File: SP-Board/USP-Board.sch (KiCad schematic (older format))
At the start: 10 parts

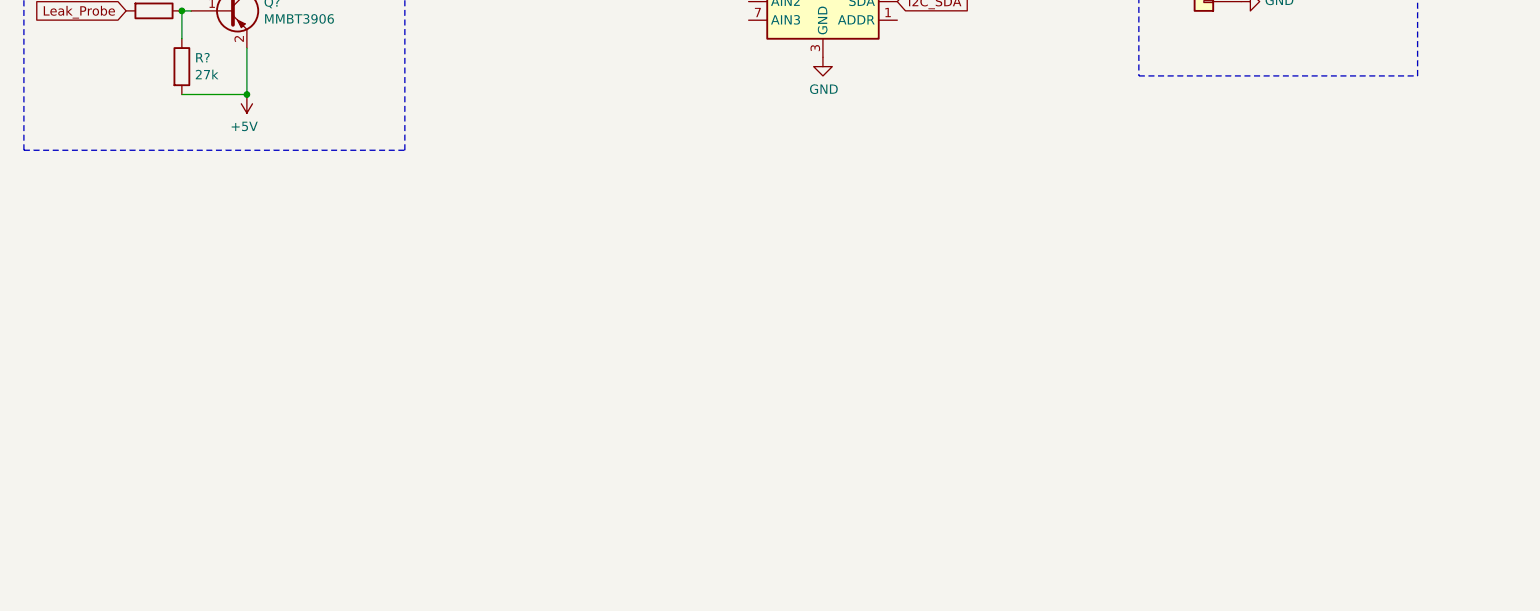
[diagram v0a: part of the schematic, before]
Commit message: Added Leak probe connectors and xt60 connector
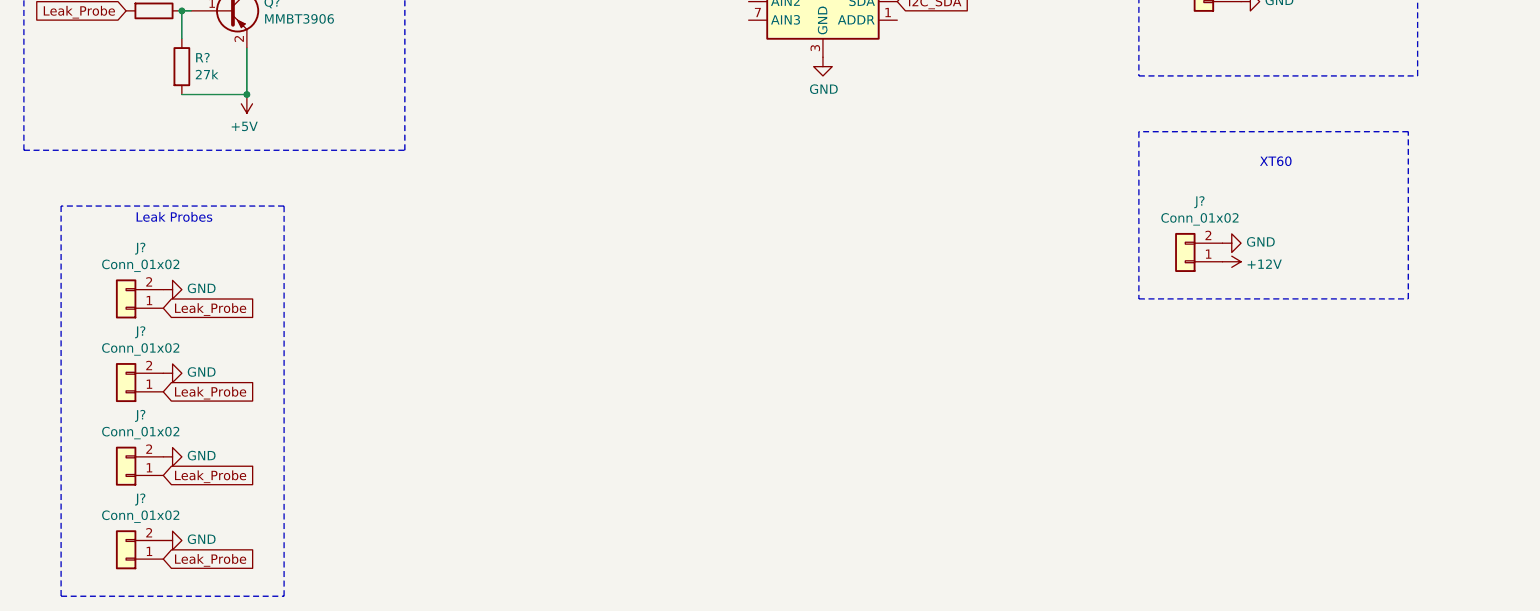
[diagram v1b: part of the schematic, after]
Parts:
- added J? (x5): Conn_01x02, symbol Connector_Generic:Conn_01x02
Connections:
- net GND: now also J?.2 (Pin_2), J?.2 (Pin_2), J?.2 (Pin_2), J?.2 (Pin_2), J?.2 (Pin_2)
- net Leak_Probe: now also J?.1 (Pin_1), J?.1 (Pin_1), J?.1 (Pin_1), J?.1 (Pin_1)
- new net +12V: J?.1 (Pin_1)
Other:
- note added: "Leak Probes\n"
- note added: "XT60\n"
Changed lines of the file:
@@
 Text Notes 7450 1350 0    50   ~ 0
 Depht/Temp\n
+$Comp
+L Connector_Generic:Conn_01x02 J?
+U 1 1 5C6F22AD
+P 7200 3450
+F 0 "J?" H 7120 3125 50  0000 C CNN
+F 1 "Conn_01x02" H 7120 3216 50  0000 C CNN
+F 2 "" H 7200 3450 50  0001 C CNN
+F 3 "~" H 7200 3450 50  0001 C CNN
+	1    7200 3450
+	-1   0    0    1
+$EndComp
+$Comp
+L power:GND #PWR?
+U 1 1 5C6F2330
+P 7400 3350
+F 0 "#PWR?" H 7400 3100 50  0001 C CNN
+F 1 "GND" V 7405 3222 50  0000 R CNN
+F 2 "" H 7400 3350 50  0001 C CNN
+F 3 "" H 7400 3350 50  0001 C CNN
+	1    7400 3350
+	0    -1   -1   0
+$EndComp
+$Comp
+L power:+12V #PWR?
+U 1 1 5C6F23A3
+P 7400 3450
+F 0 "#PWR?" H 7400 3300 50  0001 C CNN
+F 1 "+12V" V 7415 3578 50  0000 L CNN
+F 2 "" H 7400 3450 50  0001 C CNN
+F 3 "" H 7400 3450 50  0001 C CNN
+	1    7400 3450
+	0    1    1    0
+$EndComp
+Wire Notes Line
+	6950 3650 8400 3650
+Wire Notes Line
+	8400 3650 8400 2750
+Wire Notes Line
+	8400 2750 6950 2750
+Wire Notes Line
+	6950 2750 6950 3650
+Text Notes 7600 2950 0    50   ~ 0
+XT60\n
+$Comp
+L Connector_Generic:Conn_01x02 J?
+U 1 1 5C6F2A9B
+P 1500 3700
+F 0 "J?" H 1420 3375 50  0000 C CNN
+F 1 "Conn_01x02" H 1420 3466 50  0000 C CNN
+F 2 "" H 1500 3700 50  0001 C CNN
+F 3 "~" H 1500 3700 50  0001 C CNN
+	1    1500 3700
+	-1   0    0    1
+$EndComp
+$Comp
+L Connector_Generic:Conn_01x02 J?
+U 1 1 5C6F2AFB
+P 1500 4150
+F 0 "J?" H 1420 3825 50  0000 C CNN
+F 1 "Conn_01x02" H 1420 3916 50  0000 C CNN
+F 2 "" H 1500 4150 50  0001 C CNN
+F 3 "~" H 1500 4150 50  0001 C CNN
+	1    1500 4150
+	-1   0    0    1
+$EndComp
+$Comp
+L Connector_Generic:Conn_01x02 J?
+U 1 1 5C6F2B6A
+P 1500 4600
+F 0 "J?" H 1420 4275 50  0000 C CNN
+F 1 "Conn_01x02" H 1420 4366 50  0000 C CNN
+F 2 "" H 1500 4600 50  0001 C CNN
+F 3 "~" H 1500 4600 50  0001 C CNN
+	1    1500 4600
+	-1   0    0    1
+$EndComp
+$Comp
+L Connector_Generic:Conn_01x02 J?
+U 1 1 5C6F2BA4
+P 1500 5050
+F 0 "J?" H 1420 4725 50  0000 C CNN
+F 1 "Conn_01x02" H 1420 4816 50  0000 C CNN
+F 2 "" H 1500 5050 50  0001 C CNN
+F 3 "~" H 1500 5050 50  0001 C CNN
+	1    1500 5050
+	-1   0    0    1
+$EndComp
+Text GLabel 1700 3700 2    50   Input ~ 0
+Leak_Probe
+Text GLabel 1700 4150 2    50   Input ~ 0
+Leak_Probe
+Text GLabel 1700 4600 2    50   Input ~ 0
+Leak_Probe
+Text GLabel 1700 5050 2    50   Input ~ 0
+Leak_Probe
+$Comp
+L power:GND #PWR?
+U 1 1 5C6F390D
+P 1700 4500
+F 0 "#PWR?" H 1700 4250 50  0001 C CNN
+F 1 "GND" V 1705 4372 50  0000 R CNN
+F 2 "" H 1700 4500 50  0001 C CNN
+F 3 "" H 1700 4500 50  0001 C CNN
+	1    1700 4500
+	0    -1   -1   0
+$EndComp
+$Comp
+L power:GND #PWR?
+U 1 1 5C6F396A
+P 1700 4050
+F 0 "#PWR?" H 1700 3800 50  0001 C CNN
+F 1 "GND" V 1705 3922 50  0000 R CNN
+F 2 "" H 1700 4050 50  0001 C CNN
+F 3 "" H 1700 4050 50  0001 C CNN
+	1    1700 4050
+	0    -1   -1   0
+$EndComp
+$Comp
+L power:GND #PWR?
+U 1 1 5C6F3993
+P 1700 3600
+F 0 "#PWR?" H 1700 3350 50  0001 C CNN
+F 1 "GND" V 1705 3472 50  0000 R CNN
+F 2 "" H 1700 3600 50  0001 C CNN
+F 3 "" H 1700 3600 50  0001 C CNN
+	1    1700 3600
+	0    -1   -1   0
+$EndComp
+$Comp
+L power:GND #PWR?
+U 1 1 5C6F39BC
+P 1700 4950
+F 0 "#PWR?" H 1700 4700 50  0001 C CNN
+F 1 "GND" V 1705 4822 50  0000 R CNN
+F 2 "" H 1700 4950 50  0001 C CNN
+F 3 "" H 1700 4950 50  0001 C CNN
+	1    1700 4950
+	0    -1   -1   0
+$EndComp
+Wire Notes Line
+	1150 5250 2350 5250
+Wire Notes Line
+	2350 5250 2350 3150
+Wire Notes Line
+	2350 3150 1150 3150
+Wire Notes Line
+	1150 3150 1150 5250
+Text Notes 1550 3250 0    50   ~ 0
+Leak Probes\n
 $EndSCHEMATC

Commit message: moving macines
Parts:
- added C?: C_Small, symbol Device:C_Small
- added J? (x2): Conn_01x03, symbol Connector_Generic:Conn_01x03
- added J?: Conn_01x04, symbol Connector_Generic:Conn_01x04
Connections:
- net +12V: now also J?.1 (Pin_1), J?.3 (Pin_3)
- net +5V: now also U?.8 (VDD), C?.2
- net EXT_PWM_LED: now also J?.2 (Pin_2)
- net GND: now also C?.1, J?.1 (Pin_1), J?.2 (Pin_2), J?.2 (Pin_2)
- net I2C_SCL: now also J?.3 (Pin_3)
- net I2C_SDA: now also J?.4 (Pin_4)
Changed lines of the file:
@@
 U 1 1 5C6DF5CB
 P 5250 1950
-F 0 "U?" H 5250 2628 50  0000 C CNN
-F 1 "ADS1015IDGS" H 5250 2537 50  0000 C CNN
+F 0 "U?" H 4850 2650 50  0000 C CNN
+F 1 "ADS1015IDGS" H 4850 2550 50  0000 C CNN
 F 2 "Package_SO:TSSOP-10_3x3mm_P0.5mm" H 5250 1450 50  0001 C CNN
 F 3 "http://www.ti.com/lit/ds/symlink/ads1015.pdf" H 5200 1050 50  0001 C CNN
@@
 Text Notes 1550 3250 0    50   ~ 0
 Leak Probes\n
+$Comp
+L Connector_Generic:Conn_01x03 J?
+U 1 1 5C6F621E
+P 7200 4550
+F 0 "J?" H 7120 4225 50  0000 C CNN
+F 1 "Conn_01x03" H 7120 4316 50  0000 C CNN
+F 2 "" H 7200 4550 50  0001 C CNN
+F 3 "~" H 7200 4550 50  0001 C CNN
+	1    7200 4550
+	-1   0    0    1
+$EndComp
+$Comp
+L power:GND #PWR?
+U 1 1 5C6F62AC
+P 7400 4650
+F 0 "#PWR?" H 7400 4400 50  0001 C CNN
+F 1 "GND" V 7405 4522 50  0000 R CNN
+F 2 "" H 7400 4650 50  0001 C CNN
+F 3 "" H 7400 4650 50  0001 C CNN
+	1    7400 4650
+	0    -1   -1   0
+$EndComp
+$Comp
+L power:+12V #PWR?
+U 1 1 5C6F6333
+P 7400 4450
+F 0 "#PWR?" H 7400 4300 50  0001 C CNN
+F 1 "+12V" V 7415 4578 50  0000 L CNN
+F 2 "" H 7400 4450 50  0001 C CNN
+F 3 "" H 7400 4450 50  0001 C CNN
+	1    7400 4450
+	0    1    1    0
+$EndComp
+Text GLabel 7400 4550 2    50   Input ~ 0
+EXT_PWM_LED
+$Comp
+L Connector_Generic:Conn_01x04 J?
+U 1 1 5C6F63B5
+P 7200 5400
+F 0 "J?" H 7120 4975 50  0000 C CNN
+F 1 "Conn_01x04" H 7120 5066 50  0000 C CNN
+F 2 "" H 7200 5400 50  0001 C CNN
+F 3 "~" H 7200 5400 50  0001 C CNN
+	1    7200 5400
+	-1   0    0    1
+$EndComp
+Text GLabel 7400 5200 2    50   Input ~ 0
+I2C_SDA
+Text GLabel 7400 5300 2    50   Input ~ 0
+I2C_SCL
+$Comp
+L power:GND #PWR?
+U 1 1 5C6F6B79
+P 7400 5400
+F 0 "#PWR?" H 7400 5150 50  0001 C CNN
+F 1 "GND" V 7405 5272 50  0000 R CNN
+F 2 "" H 7400 5400 50  0001 C CNN
+F 3 "" H 7400 5400 50  0001 C CNN
+	1    7400 5400
+	0    -1   -1   0
+$EndComp
+$Comp
+L power:+12V #PWR?
+U 1 1 5C6F6BA6
+P 7400 5500
+F 0 "#PWR?" H 7400 5350 50  0001 C CNN
+F 1 "+12V" V 7415 5628 50  0000 L CNN
+F 2 "" H 7400 5500 50  0001 C CNN
+F 3 "" H 7400 5500 50  0001 C CNN
+	1    7400 5500
+	0    1    1    0
+$EndComp
+$Comp
+L Connector_Generic:Conn_01x03 J?
+U 1 1 5C6F7BD4
+P 7200 6050
+F 0 "J?" H 7120 5725 50  0000 C CNN
+F 1 "Conn_01x03" H 7120 5816 50  0000 C CNN
+F 2 "" H 7200 6050 50  0001 C CNN
+F 3 "~" H 7200 6050 50  0001 C CNN
+	1    7200 6050
+	-1   0    0    1
+$EndComp
+$Comp
+L power:GND #PWR?
+U 1 1 5C6F7CC0
+P 7400 6050
+F 0 "#PWR?" H 7400 5800 50  0001 C CNN
+F 1 "GND" V 7400 5850 50  0000 C CNN
+F 2 "" H 7400 6050 50  0001 C CNN
+F 3 "" H 7400 6050 50  0001 C CNN
+	1    7400 6050
+	0    -1   -1   0
+$EndComp
+$Comp
+L Device:C_Small C?
+U 1 1 5C6F8556
+P 5250 1250
+F 0 "C?" H 5342 1296 50  0000 L CNN
+F 1 "C_Small" H 5342 1205 50  0000 L CNN
+F 2 "" H 5250 1250 50  0001 C CNN
+F 3 "~" H 5250 1250 50  0001 C CNN
+	1    5250 1250
+	1    0    0    -1
+$EndComp
+Wire Wire Line
+	5250 1350 5250 1400
+$Comp
+L power:GND #PWR?
+U 1 1 5C6F8BB7
+P 5250 1150
+F 0 "#PWR?" H 5250 900 50  0001 C CNN
+F 1 "GND" H 5255 977 50  0000 C CNN
+F 2 "" H 5250 1150 50  0001 C CNN
+F 3 "" H 5250 1150 50  0001 C CNN
+	1    5250 1150
+	-1   0    0    1
+$EndComp
+$Comp
+L power:+5V #PWR?
+U 1 1 5C6F8C33
+P 5450 1400
+F 0 "#PWR?" H 5450 1250 50  0001 C CNN
+F 1 "+5V" V 5465 1528 50  0000 L CNN
+F 2 "" H 5450 1400 50  0001 C CNN
+F 3 "" H 5450 1400 50  0001 C CNN
+	1    5450 1400
+	0    1    1    0
+$EndComp
+Wire Wire Line
+	5450 1400 5250 1400
+Connection ~ 5250 1400
+Wire Wire Line
+	5250 1400 5250 1450
 $EndSCHEMATC

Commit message: Udated ADC 90% complete
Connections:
- net I2C_SDA: now also U?.1 (ADDR)
- net Leak_Sig: now also U?.5 (AIN1)
- net ANLG_Induction_SENS: now reaches U?.4 (AIN0)
- net ANLG_Induction_SENS: now also J?.3 (Pin_3)
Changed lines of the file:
@@
 Wire Wire Line
 	5250 1400 5250 1450
+Text GLabel 5650 2150 2    50   Input ~ 0
+I2C_SDA
+Text GLabel 7400 5950 2    50   Input ~ 0
+ANLG_Induction_SENS
+Text GLabel 4850 1850 0    50   Input ~ 0
+ANLG_Induction_SENS
+Text GLabel 4850 1950 0    50   Input ~ 0
+Leak_Sig
 $EndSCHEMATC

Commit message: backup
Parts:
- added H1, H2, H3, H4: MountingHole, MountingHole:MountingHole_3mm_Pad, symbol Mechanical:MountingHole
- J10, J11: renamed from J?; footprint (none) -> Blue_ESC:RJ45_8
- gave numbers to parts that had none: 17

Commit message: More sch updates
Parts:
- added C2, C3, C4, C5, C6: 1uF, symbol Device:CP
- added U2: MAX232, symbol Interface_UART:MAX232
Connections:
- net +5V: now also J8.1 (Pin_1)
- net GND: now also J8.3 (Pin_3), C3.2, C6.1, U2.15 (GND); no longer J8.2 (Pin_2)
- net ANLG_Induction_SENS renamed ANLG_HAL_SENS
- net ANLG_HAL_SENS: now also J8.2 (Pin_2); no longer J8.3 (Pin_3)
- new net: C2.1, U2.1 (C1+)
- new net: C3.1, C4.2, U2.16 (VCC)
- new net: C4.1, U2.2 (VS+)
- new net: C2.2, U2.3 (C1-)
- new net: C5.1, U2.4 (C2+)
- new net: C5.2, U2.5 (C2-)
- new net: C6.2, U2.6 (VS-)
- no-connect marks 0 -> 3
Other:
- moved on the sheet: H1, H2, H3, H4
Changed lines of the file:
@@
 L power:GND #PWR0122
 U 1 1 5C6F7CC0
-P 7400 6050
-F 0 "#PWR0122" H 7400 5800 50  0001 C CNN
-F 1 "GND" V 7400 5850 50  0000 C CNN
-F 2 "" H 7400 6050 50  0001 C CNN
-F 3 "" H 7400 6050 50  0001 C CNN
-	1    7400 6050
+P 7400 5950
+F 0 "#PWR0122" H 7400 5700 50  0001 C CNN
+F 1 "GND" V 7400 5750 50  0000 C CNN
+F 2 "" H 7400 5950 50  0001 C CNN
+F 3 "" H 7400 5950 50  0001 C CNN
+	1    7400 5950
 	0    -1   -1   0
 $EndComp
@@
 Text GLabel 5650 2150 2    50   Input ~ 0
 I2C_SDA
-Text GLabel 7400 5950 2    50   Input ~ 0
-ANLG_Induction_SENS
+Text GLabel 7400 6050 2    50   Input ~ 0
+ANLG_HAL_SENS
 Text GLabel 4850 1850 0    50   Input ~ 0
-ANLG_Induction_SENS
+ANLG_HAL_SENS
 Text GLabel 4850 1950 0    50   Input ~ 0
 Leak_Sig
@@
 L Mechanical:MountingHole H1
 U 1 1 5C84499E
-P 4750 4950
-F 0 "H1" H 4850 4996 50  0000 L CNN
-F 1 "MountingHole" H 4850 4905 50  0000 L CNN
-F 2 "MountingHole:MountingHole_3mm_Pad" H 4750 4950 50  0001 C CNN
-F 3 "~" H 4750 4950 50  0001 C CNN
-	1    4750 4950
+P 1200 6150
+F 0 "H1" H 1300 6196 50  0000 L CNN
+F 1 "MountingHole" H 1300 6105 50  0000 L CNN
+F 2 "MountingHole:MountingHole_3mm_Pad" H 1200 6150 50  0001 C CNN
+F 3 "~" H 1200 6150 50  0001 C CNN
+	1    1200 6150
 	1    0    0    -1
 $EndComp
@@
 L Mechanical:MountingHole H2
 U 1 1 5C8449DE
-P 4750 5300
-F 0 "H2" H 4850 5346 50  0000 L CNN
-F 1 "MountingHole" H 4850 5255 50  0000 L CNN
-F 2 "MountingHole:MountingHole_3mm_Pad" H 4750 5300 50  0001 C CNN
-F 3 "~" H 4750 5300 50  0001 C CNN
-	1    4750 5300
+P 1200 6500
+F 0 "H2" H 1300 6546 50  0000 L CNN
+F 1 "MountingHole" H 1300 6455 50  0000 L CNN
+F 2 "MountingHole:MountingHole_3mm_Pad" H 1200 6500 50  0001 C CNN
+F 3 "~" H 1200 6500 50  0001 C CNN
+	1    1200 6500
 	1    0    0    -1
 $EndComp
@@
 L Mechanical:MountingHole H3
 U 1 1 5C844A42
-P 4750 5700
-F 0 "H3" H 4850 5746 50  0000 L CNN
-F 1 "MountingHole" H 4850 5655 50  0000 L CNN
-F 2 "MountingHole:MountingHole_3mm_Pad" H 4750 5700 50  0001 C CNN
-F 3 "~" H 4750 5700 50  0001 C CNN
-	1    4750 5700
+P 1200 6900
+F 0 "H3" H 1300 6946 50  0000 L CNN
+F 1 "MountingHole" H 1300 6855 50  0000 L CNN
+F 2 "MountingHole:MountingHole_3mm_Pad" H 1200 6900 50  0001 C CNN
+F 3 "~" H 1200 6900 50  0001 C CNN
+	1    1200 6900
 	1    0    0    -1
 $EndComp
@@
 L Mechanical:MountingHole H4
 U 1 1 5C844AA4
-P 4750 6000
-F 0 "H4" H 4850 6046 50  0000 L CNN
-F 1 "MountingHole" H 4850 5955 50  0000 L CNN
-F 2 "MountingHole:MountingHole_3mm_Pad" H 4750 6000 50  0001 C CNN
-F 3 "~" H 4750 6000 50  0001 C CNN
-	1    4750 6000
-	1    0    0    -1
-$EndComp
+P 1200 7200
+F 0 "H4" H 1300 7246 50  0000 L CNN
+F 1 "MountingHole" H 1300 7155 50  0000 L CNN
+F 2 "MountingHole:MountingHole_3mm_Pad" H 1200 7200 50  0001 C CNN
+F 3 "~" H 1200 7200 50  0001 C CNN
+	1    1200 7200
+	1    0    0    -1
+$EndComp
+$Comp
+L power:+5V #PWR0125
+U 1 1 5C998D8E
+P 7400 6150
+F 0 "#PWR0125" H 7400 6000 50  0001 C CNN
+F 1 "+5V" V 7415 6278 50  0000 L CNN
+F 2 "" H 7400 6150 50  0001 C CNN
+F 3 "" H 7400 6150 50  0001 C CNN
+	1    7400 6150
+	0    1    1    0
+$EndComp
+NoConn ~ 5650 1750
+NoConn ~ 4850 2050
+NoConn ~ 4850 2150
+$Comp
+L Interface_UART:MAX232 U2
+U 1 1 5C99D6CE
+P 4250 5750
+F 0 "U2" H 4000 4700 50  0000 C CNN
+F 1 "MAX232" H 4050 6800 50  0000 C CNN
+F 2 "" H 4300 4700 50  0001 L CNN
+F 3 "http://www.ti.com/lit/ds/symlink/max232.pdf" H 4250 5850 50  0001 C CNN
+	1    4250 5750
+	1    0    0    -1
+$EndComp
+$Comp
+L Device:CP C2
+U 1 1 5C99E1C6
+P 3250 5000
+F 0 "C2" H 3368 5046 50  0000 L CNN
+F 1 "1uF" H 3368 4955 50  0000 L CNN
+F 2 "" H 3288 4850 50  0001 C CNN
+F 3 "~" H 3250 5000 50  0001 C CNN
+	1    3250 5000
+	1    0    0    -1
+$EndComp
+Wire Wire Line
+	3450 4850 3250 4850
+Wire Wire Line
+	3250 5150 3450 5150
+$Comp
+L power:GND #PWR0126
+U 1 1 5C99E75A
+P 4250 6950
+F 0 "#PWR0126" H 4250 6700 50  0001 C CNN
+F 1 "GND" H 4255 6777 50  0000 C CNN
+F 2 "" H 4250 6950 50  0001 C CNN
+F 3 "" H 4250 6950 50  0001 C CNN
+	1    4250 6950
+	1    0    0    -1
+$EndComp
+$Comp
+L Device:CP C6
+U 1 1 5C99E79E
+P 5750 5650
+F 0 "C6" V 5495 5650 50  0000 C CNN
+F 1 "1uF" V 5586 5650 50  0000 C CNN
+F 2 "" H 5788 5500 50  0001 C CNN
+F 3 "~" H 5750 5650 50  0001 C CNN
+	1    5750 5650
+	0    1    1    0
+$EndComp
+Wire Wire Line
+	5600 5650 5050 5650
+$Comp
+L power:GND #PWR0127
+U 1 1 5C99EAE5
+P 5900 5650
+F 0 "#PWR0127" H 5900 5400 50  0001 C CNN
+F 1 "GND" H 5905 5477 50  0000 C CNN
+F 2 "" H 5900 5650 50  0001 C CNN
+F 3 "" H 5900 5650 50  0001 C CNN
+	1    5900 5650
+	1    0    0    -1
+$EndComp
+$Comp
+L power:GND #PWR0128
+U 1 1 5C99EB24
+P 3250 4200
+F 0 "#PWR0128" H 3250 3950 50  0001 C CNN
+F 1 "GND" H 3255 4027 50  0000 C CNN
+F 2 "" H 3250 4200 50  0001 C CNN
+F 3 "" H 3250 4200 50  0001 C CNN
+	1    3250 4200
+	1    0    0    -1
+$EndComp
+$Comp
+L Device:CP C5
+U 1 1 5C99EB63
+P 5200 5000
+F 0 "C5" H 5318 5046 50  0000 L CNN
+F 1 "1uF" H 5318 4955 50  0000 L CNN
+F 2 "" H 5238 4850 50  0001 C CNN
+F 3 "~" H 5200 5000 50  0001 C CNN
+	1    5200 5000
+	1    0    0    -1
+$EndComp
+Wire Wire Line
+	5200 4850 5050 4850
+Wire Wire Line
+	5200 5150 5050 5150
+Wire Wire Line
+	5050 5350 5550 5350
+Wire Wire Line
+	5550 5350 5550 4200
+Wire Wire Line
+	5550 4200 4850 4200
+$Comp
+L Device:CP C4
+U 1 1 5C99F2B9
+P 4700 4200
+F 0 "C4" V 4445 4200 50  0000 C CNN
+F 1 "1uF" V 4536 4200 50  0000 C CNN
+F 2 "" H 4738 4050 50  0001 C CNN
+F 3 "~" H 4700 4200 50  0001 C CNN
+	1    4700 4200
+	0    1    1    0
+$EndComp
+Wire Wire Line
+	4250 4550 4250 4200
+Wire Wire Line
+	4250 4200 4550 4200
+$Comp
+L Device:CP C3
+U 1 1 5C99F6D7
+P 3400 4200
+F 0 "C3" V 3145 4200 50  0000 C CNN
+F 1 "1uF" V 3236 4200 50  0000 C CNN
+F 2 "" H 3438 4050 50  0001 C CNN
+F 3 "~" H 3400 4200 50  0001 C CNN
+	1    3400 4200
+	0    1    1    0
+$EndComp
+Wire Wire Line
+	3550 4200 4250 4200
+Connection ~ 4250 4200
 $EndSCHEMATC

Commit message: Early Footprint
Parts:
- C2, C3, C4, C5, C6: footprint (none) -> Capacitor_Tantalum_SMD:CP_EIA-1608-08_AVX-J_Pad1.25x1.05mm_HandSolder
- D1: footprint (none) -> LED_SMD:LED_0603_1608Metric
- R1, R2, R3: footprint (none) -> Resistor_SMD:R_1206_3216Metric_Pad1.42x1.75mm_HandSolder
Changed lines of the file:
@@
 F 0 "R1" V 1443 2100 50  0000 C CNN
 F 1 "1k" V 1534 2100 50  0000 C CNN
-F 2 "" V 1580 2100 50  0001 C CNN
+F 2 "Resistor_SMD:R_1206_3216Metric_Pad1.42x1.75mm_HandSolder" V 1580 2100 50  0001 C CNN
 F 3 "~" H 1650 2100 50  0001 C CNN
 	1    1650 2100
@@
 F 0 "R2" H 1870 2446 50  0000 L CNN
 F 1 "27k" H 1870 2355 50  0000 L CNN
-F 2 "" V 1730 2400 50  0001 C CNN
+F 2 "Resistor_SMD:R_1206_3216Metric_Pad1.42x1.75mm_HandSolder" V 1730 2400 50  0001 C CNN
 F 3 "~" H 1800 2400 50  0001 C CNN
 	1    1800 2400
@@
 F 0 "R3" H 2080 1504 50  0000 R CNN
 F 1 "1k" H 2080 1595 50  0000 R CNN
-F 2 "" V 2080 1550 50  0001 C CNN
+F 2 "Resistor_SMD:R_1206_3216Metric_Pad1.42x1.75mm_HandSolder" V 2080 1550 50  0001 C CNN
 F 3 "~" H 2150 1550 50  0001 C CNN
 	1    2150 1550
@@
 F 0 "D1" V 2395 1328 50  0000 L CNN
 F 1 "LED" V 2486 1328 50  0000 L CNN
-F 2 "" H 2450 1250 50  0001 C CNN
+F 2 "LED_SMD:LED_0603_1608Metric" H 2450 1250 50  0001 C CNN
 F 3 "~" H 2450 1250 50  0001 C CNN
 	1    2450 1250
@@
 F 0 "C2" H 3368 5046 50  0000 L CNN
 F 1 "1uF" H 3368 4955 50  0000 L CNN
-F 2 "" H 3288 4850 50  0001 C CNN
+F 2 "Capacitor_Tantalum_SMD:CP_EIA-1608-08_AVX-J_Pad1.25x1.05mm_HandSolder" H 3288 4850 50  0001 C CNN
 F 3 "~" H 3250 5000 50  0001 C CNN
 	1    3250 5000
@@
 F 0 "C6" V 5495 5650 50  0000 C CNN
 F 1 "1uF" V 5586 5650 50  0000 C CNN
-F 2 "" H 5788 5500 50  0001 C CNN
+F 2 "Capacitor_Tantalum_SMD:CP_EIA-1608-08_AVX-J_Pad1.25x1.05mm_HandSolder" H 5788 5500 50  0001 C CNN
 F 3 "~" H 5750 5650 50  0001 C CNN
 	1    5750 5650
@@
 F 0 "C5" H 5318 5046 50  0000 L CNN
 F 1 "1uF" H 5318 4955 50  0000 L CNN
-F 2 "" H 5238 4850 50  0001 C CNN
+F 2 "Capacitor_Tantalum_SMD:CP_EIA-1608-08_AVX-J_Pad1.25x1.05mm_HandSolder" H 5238 4850 50  0001 C CNN
 F 3 "~" H 5200 5000 50  0001 C CNN
 	1    5200 5000
@@
 F 0 "C4" V 4445 4200 50  0000 C CNN
 F 1 "1uF" V 4536 4200 50  0000 C CNN
-F 2 "" H 4738 4050 50  0001 C CNN
+F 2 "Capacitor_Tantalum_SMD:CP_EIA-1608-08_AVX-J_Pad1.25x1.05mm_HandSolder" H 4738 4050 50  0001 C CNN
 F 3 "~" H 4700 4200 50  0001 C CNN
 	1    4700 4200
@@
 F 0 "C3" V 3145 4200 50  0000 C CNN
 F 1 "1uF" V 3236 4200 50  0000 C CNN
-F 2 "" H 3438 4050 50  0001 C CNN
+F 2 "Capacitor_Tantalum_SMD:CP_EIA-1608-08_AVX-J_Pad1.25x1.05mm_HandSolder" H 3438 4050 50  0001 C CNN
 F 3 "~" H 3400 4200 50  0001 C CNN
 	1    3400 4200
